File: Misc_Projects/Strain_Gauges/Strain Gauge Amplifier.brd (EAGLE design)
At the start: 48.3 x 20.3 mm, 19 parts, among them IC1 INS_OPAMP_AD8221

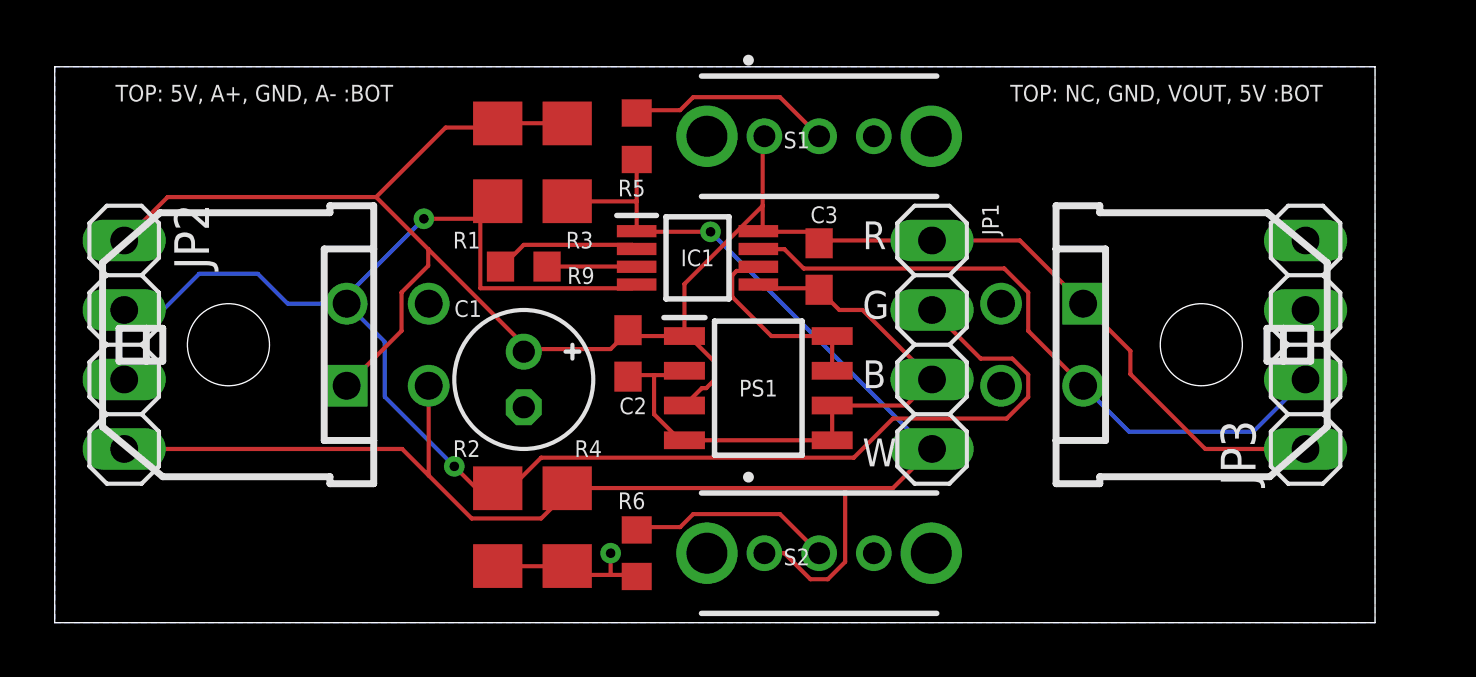
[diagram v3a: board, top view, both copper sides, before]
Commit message: changed strain gauge board connectors to microfit
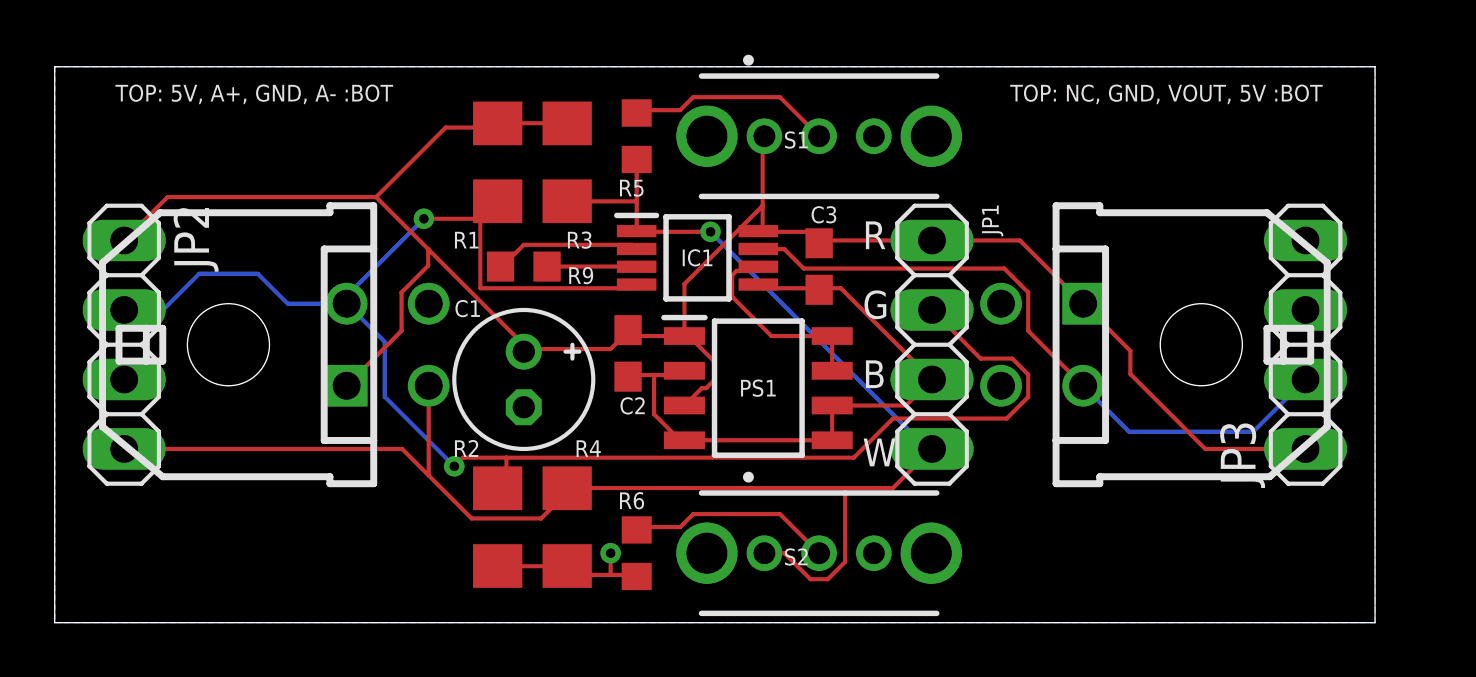
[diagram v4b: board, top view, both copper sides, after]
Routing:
- net A+: track 61.2 -> 61.7 mm
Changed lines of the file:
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@@
 <wire x1="21.11375" y1="12.22375" x2="21.27" y2="12.36" width="0.1524" layer="1"/>
 <wire x1="16.1925" y1="15.39875" x2="16.1925" y2="15.4055" width="0.1524" layer="1"/>
-<wire x1="30.63875" y1="7.46125" x2="29.21" y2="6.0325" width="0.1524" layer="1"/>
-<wire x1="17.78" y1="6.0325" x2="29.21" y2="6.0325" width="0.1524" layer="1"/>
+<wire x1="29.21" y1="6.0325" x2="30.63875" y2="7.46125" width="0.1524" layer="1"/>
 <wire x1="15.5575" y1="14.76375" x2="16.1925" y2="15.4055" width="0.1524" layer="1"/>
 <contactref element="JP2" pad="2"/>
@@
 <wire x1="35.5836" y1="8.24843125" x2="34.79641875" y2="7.46125" width="0.1524" layer="1"/>
 <wire x1="34.79641875" y1="7.46125" x2="30.63875" y2="7.46125" width="0.1524" layer="1"/>
-<wire x1="16.1925" y1="4.9145" x2="16.1925" y2="4.92125" width="0.1524" layer="1"/>
-<wire x1="16.662" y1="4.9145" x2="17.78" y2="6.0325" width="0.1524" layer="1"/>
-<wire x1="16.1925" y1="4.9145" x2="16.51" y2="4.9145" width="0.1524" layer="1"/>
-<wire x1="16.51" y1="4.9145" x2="16.662" y2="4.9145" width="0.1524" layer="1"/>
 <wire x1="10.67" y1="11.66" x2="12.065" y2="10.265" width="0.1524" layer="16"/>
 <wire x1="12.065" y1="10.265" x2="12.065" y2="8.255" width="0.1524" layer="16"/>
 <via x="14.605" y="5.715" extent="1-16" drill="0.35"/>
-<wire x1="15.4055" y1="4.9145" x2="16.1925" y2="4.9145" width="0.1524" layer="1"/>
 <wire x1="12.065" y1="8.255" x2="14.605" y2="5.715" width="0.1524" layer="16"/>
-<wire x1="14.605" y1="5.715" x2="15.4055" y2="4.9145" width="0.1524" layer="1"/>
+<wire x1="14.605" y1="5.715" x2="14.9225" y2="6.0325" width="0.1524" layer="1"/>
+<wire x1="14.9225" y1="6.0325" x2="16.51" y2="6.0325" width="0.1524" layer="1"/>
+<wire x1="16.51" y1="6.0325" x2="29.21" y2="6.0325" width="0.1524" layer="1"/>
+<wire x1="16.51" y1="6.0325" x2="16.51" y2="5.232" width="0.1524" layer="1"/>
+<wire x1="16.51" y1="5.232" x2="16.1925" y2="4.9145" width="0.1524" layer="1"/>
 </signal>
 <signal name="A-">
@@
 <wire x1="25.87625" y1="17.78" x2="25.94" y2="17.78" width="0.1524" layer="1"/>
 <wire x1="32.0675" y1="13.97" x2="27.94" y2="13.97" width="0.1524" layer="1"/>
-<wire x1="32.0675" y1="13.97" x2="32.22625" y2="13.97" width="0.1524" layer="1"/>
 <wire x1="27.6225" y1="14.2875" x2="25.87625" y2="14.2875" width="0.1524" layer="1"/>
 <wire x1="27.94" y1="13.97" x2="27.6225" y2="14.2875" width="0.1524" layer="1"/>
@@
 <wire x1="13.6525" y1="13.04766875" x2="12.6764" y2="12.07156875" width="0.1524" layer="1"/>
 <wire x1="12.6764" y1="12.07156875" x2="12.6764" y2="10.6664" width="0.1524" layer="1"/>
-<wire x1="32.0675" y1="13.97" x2="35.28" y2="13.97" width="0.1524" layer="1"/>
 <wire x1="35.28" y1="13.97" x2="37.59" y2="11.66" width="0.1524" layer="1"/>
 <wire x1="37.59" y1="11.66" x2="39.3178" y2="9.9322" width="0.1524" layer="1"/>
@@
 <wire x1="39.3178" y1="9.086275" x2="42.054075" y2="6.35" width="0.1524" layer="1"/>
 <wire x1="42.054075" y1="6.35" x2="45.72" y2="6.35" width="0.1524" layer="1"/>
+<wire x1="32.0675" y1="13.97" x2="35.28" y2="13.97" width="0.1524" layer="1"/>
 </signal>
 <signal name="GND">
@@
 <wire x1="27.94" y1="12.22375" x2="27.94" y2="12.1675" width="0.1524" layer="1"/>
 <wire x1="25.87625" y1="12.22375" x2="25.72" y2="12.36" width="0.1524" layer="1"/>
-<wire x1="27.94" y1="12.065" x2="27.94" y2="12.1675" width="0.1524" layer="1"/>
 <wire x1="20.32" y1="2.54" x2="20.32" y2="1.74625" width="0.1524" layer="1"/>
-<wire x1="28.575" y1="7.9375" x2="28.4175" y2="7.9375" width="0.1524" layer="1"/>
 <via x="20.32" y="2.54" extent="1-16" drill="0.35"/>
 <contactref element="JP2" pad="3"/>
@@
 <contactref element="X1" pad="P$4"/>
 <contactref element="X2" pad="P$4"/>
-<wire x1="28.4175" y1="7.9375" x2="31.115" y2="7.9375" width="0.1524" layer="1"/>
-<wire x1="31.115" y1="7.9375" x2="32.0675" y2="8.89" width="0.1524" layer="1"/>
-<wire x1="27.94" y1="12.1675" x2="28.6775" y2="11.43" width="0.1524" layer="1"/>
-<wire x1="29.5275" y1="11.43" x2="32.0675" y2="8.89" width="0.1524" layer="1"/>
-<wire x1="28.6775" y1="11.43" x2="29.5275" y2="11.43" width="0.1524" layer="1"/>
+<wire x1="32.0675" y1="8.89" x2="31.115" y2="7.9375" width="0.1524" layer="1"/>
+<wire x1="31.115" y1="7.9375" x2="28.4175" y2="7.9375" width="0.1524" layer="1"/>
+<wire x1="28.73375" y1="12.22375" x2="27.94" y2="12.22375" width="0.1524" layer="1"/>
+<wire x1="32.0675" y1="8.89" x2="28.73375" y2="12.22375" width="0.1524" layer="1"/>
 </signal>
 <signal name="N$2">
